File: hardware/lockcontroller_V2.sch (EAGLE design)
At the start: 106 parts, among them IC1 ATMEGA644A, IC2 L6201, IC3 MAX487CSA, IC4 MAX705CSA, IC5 REF3040, IC6 LM2594, K1 G2R, K2 G2R, X2 MKDSN1,5/3-5,08, X3 MKDSN1,5/3-5,08, X9 MKDSN1,5/4-5,08

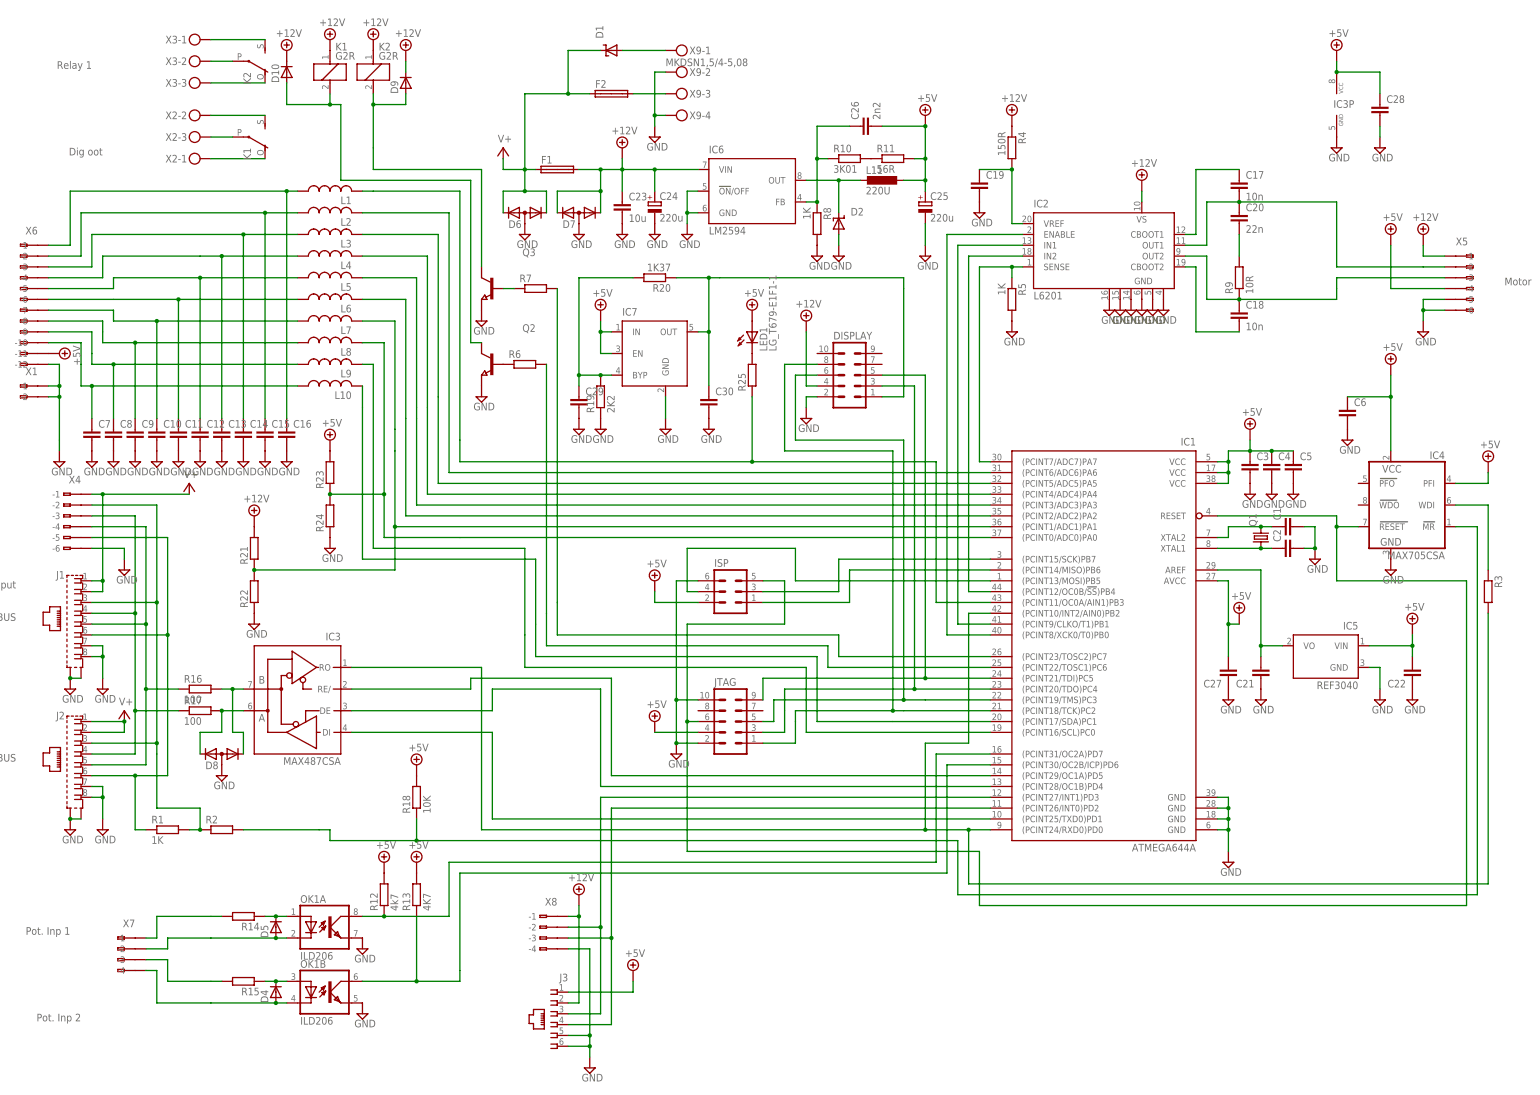
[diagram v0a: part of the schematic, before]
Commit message: fix(lockcontroller_V2): Add schematic
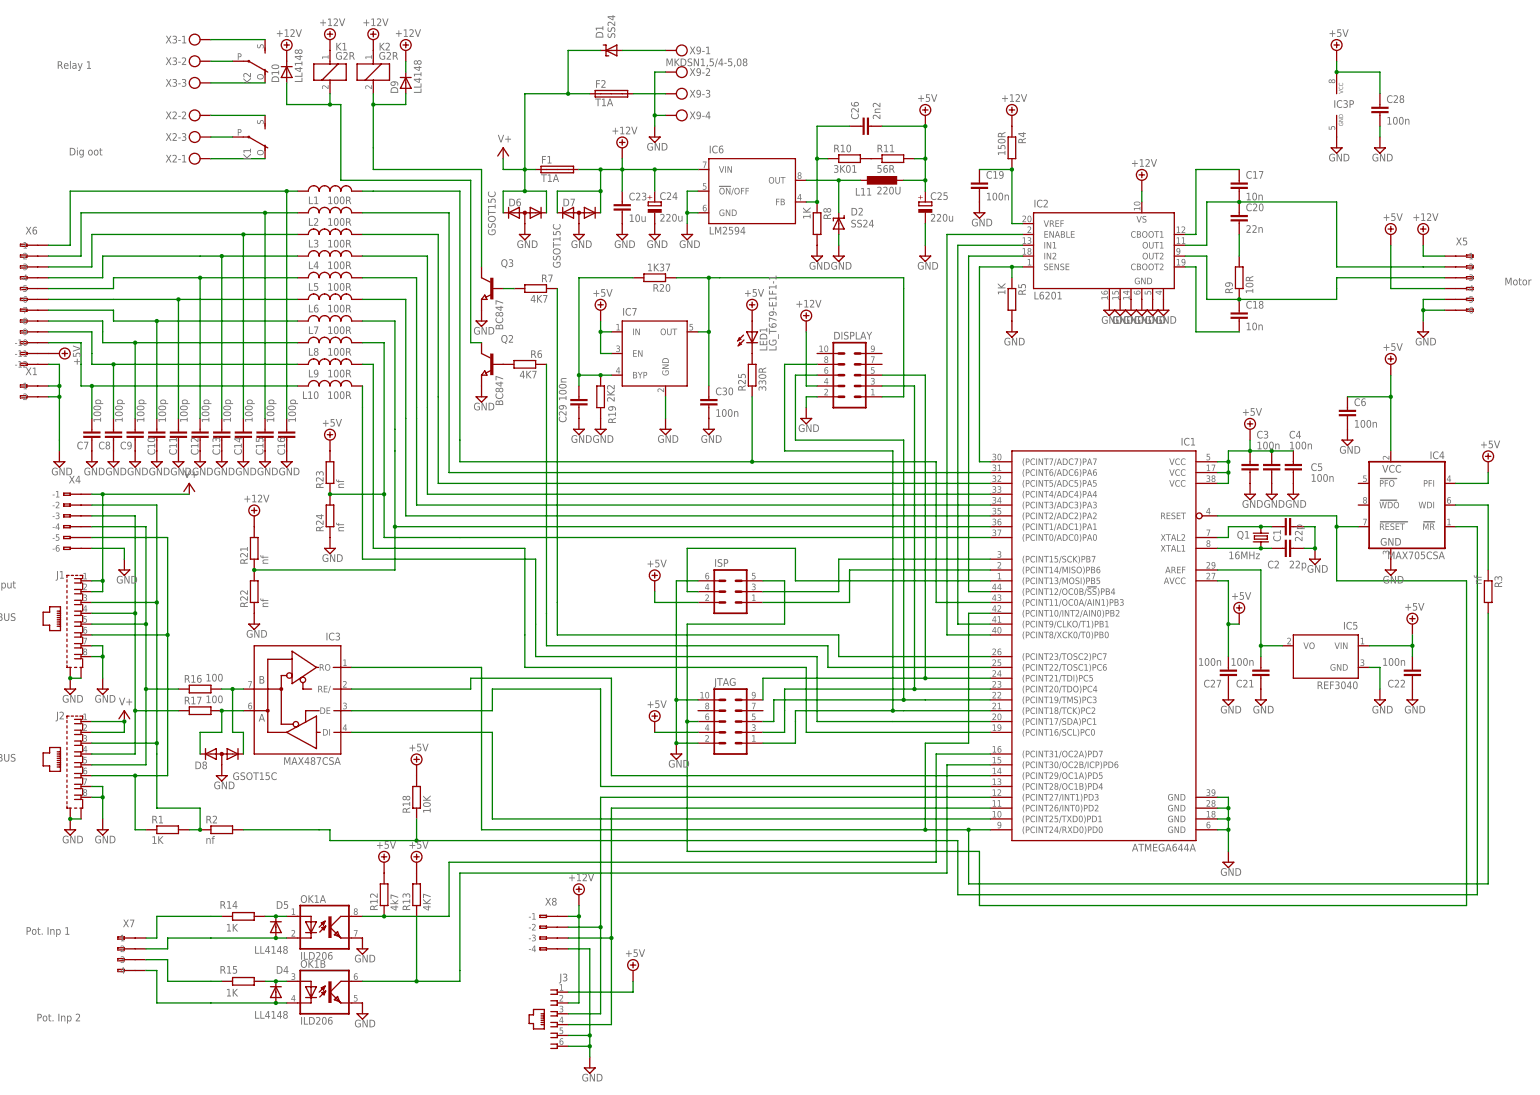
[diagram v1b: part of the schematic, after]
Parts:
- C1, C2: value (none) -> 22p
- C10, C11, C12, C13, C14, C15, C16, C7, C8, C9: value (none) -> 100p
- C19, C21, C22, C27, C28, C29, C3, C30, C4, C5, C6: value (none) -> 100n
- D1, D2: value (none) -> SS24
- D10, D4, D5, D9: value (none) -> LL4148
- D6, D7, D8: value (none) -> GSOT15C
- F1, F2: value (none) -> T1A
- L1, L10, L2, L3, L4, L5, L6, L7, L8, L9: value (none) -> 100R
- Q1: value (none) -> 16MHz
- Q2, Q3: value (none) -> BC847
- R14, R15: value (none) -> 1K
- R2, R21, R22, R23, R24, R3: value (none) -> nf
- R25: value (none) -> 330R
- R6, R7: value (none) -> 4K7
